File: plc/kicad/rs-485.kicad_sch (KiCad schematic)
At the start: 10 parts, among them CN12 DB2ERC-5.08-4P, SW5 MSK12C02, U19 THVD1450DR

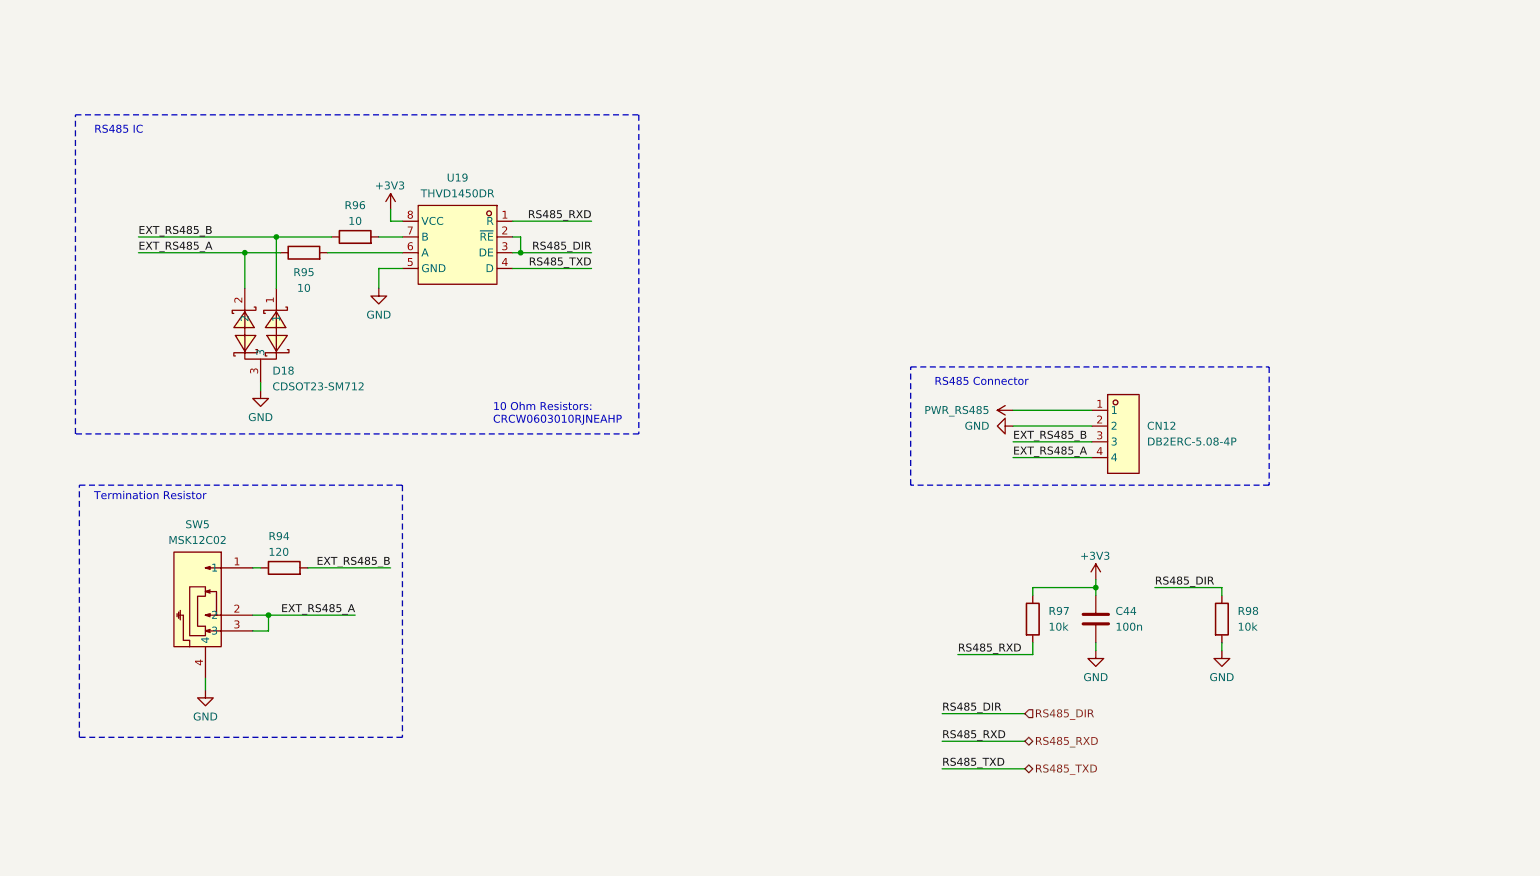
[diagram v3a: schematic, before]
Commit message: Added isolated RS-485
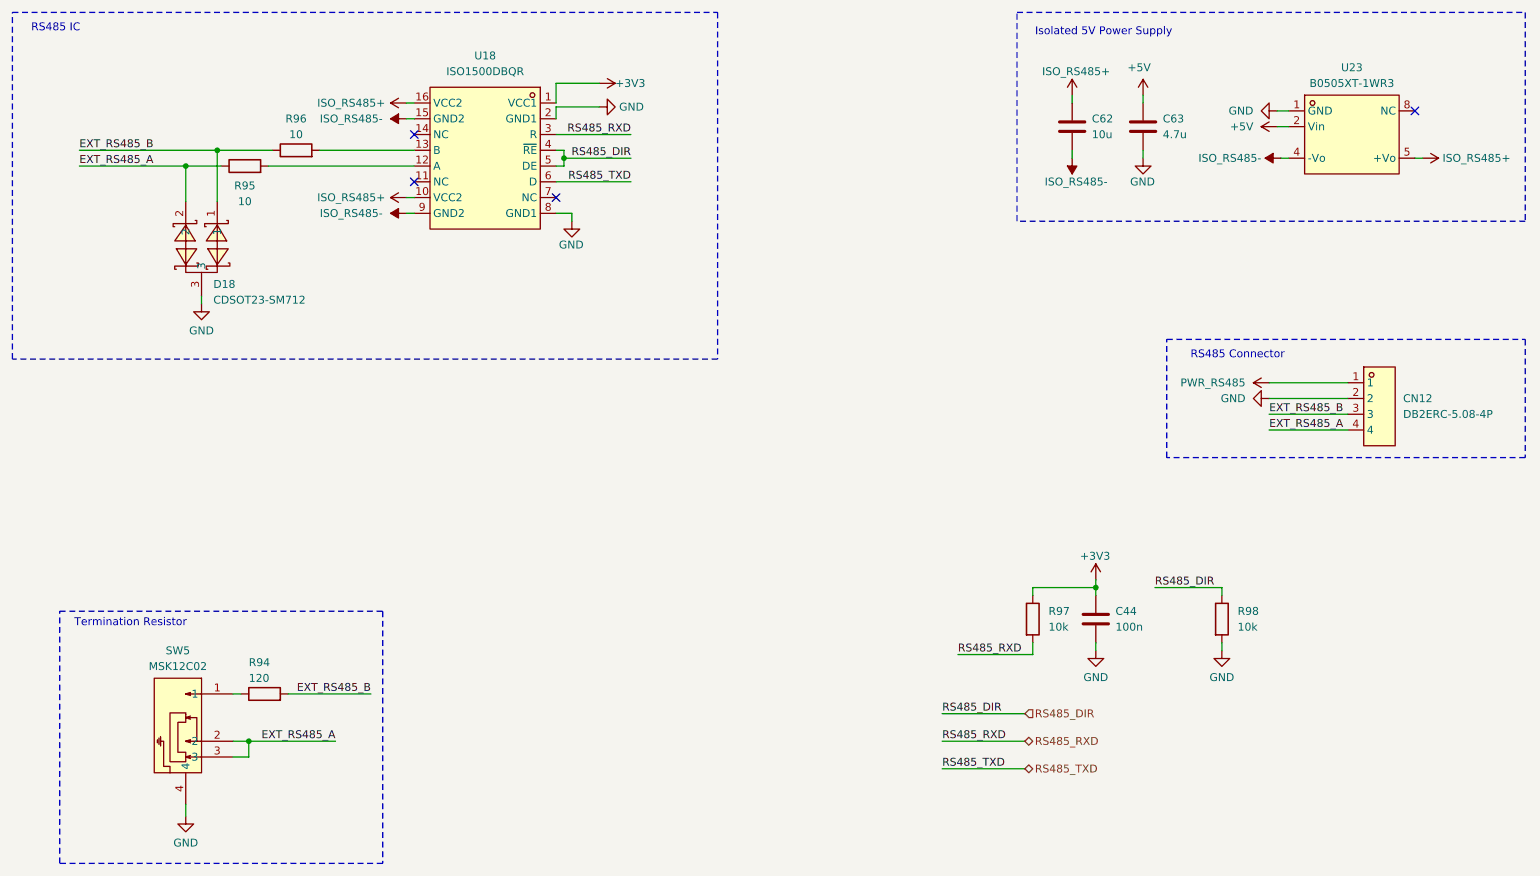
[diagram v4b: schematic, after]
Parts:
- removed U19: THVD1450DR, LibrePLC32:SOIC-8_L4.9-W3.9-P1.27-LS6.0-BL, symbol LibrePLC32:THVD1450DR
- added C62: 10u, Capacitor_SMD:C_0603_1608Metric, symbol Device:C
- added C63: 4.7u, Capacitor_SMD:C_0603_1608Metric, symbol Device:C
- added U18: ISO1500DBQR, LibrePLC32:SSOP-16_L4.9-W3.9-P0.64-LS6.0-BL, symbol LibrePLC32:ISO1500DBQR
- added U23: B0505XT-1WR3, LibrePLC32:PWRM-SMD_BXXXXXT-1WR3, symbol LibrePLC32:B0505XT-1WR3_C5369529
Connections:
- net +3V3: now also U18.1 (VCC1)
- net GND: now also C63.2, U18.2 (GND1), U18.8 (GND1), U23.1 (GND)
- net RS485_DIR: now also U18.4 (~{RE}), U18.5 (DE)
- net RS485_RXD: now also U18.3 (R)
- net RS485_TXD: now also U18.6 (D)
- net at R96.2: now also U18.13 (B)
- net at R95.2: now also U18.12 (A)
- new net +5V: C63.1, U23.2 (Vin)
- new net ISO_RS485+: C62.1, U18.10 (VCC2), U18.16 (VCC2), U23.5 (+Vo)
- new net ISO_RS485-: C62.2, U18.15 (GND2), U18.9 (GND2), U23.4 (-Vo)
- no-connect marks 0 -> 4
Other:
- note added: "Isolated 5V Power Supply"
- note removed: "10 Ohm Resistors: CRCW0603010RJNEAHP"
- moved on the sheet: CN12, D18, R94, R95, R96, SW5
